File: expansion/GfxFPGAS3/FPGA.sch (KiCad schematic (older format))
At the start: 6 parts

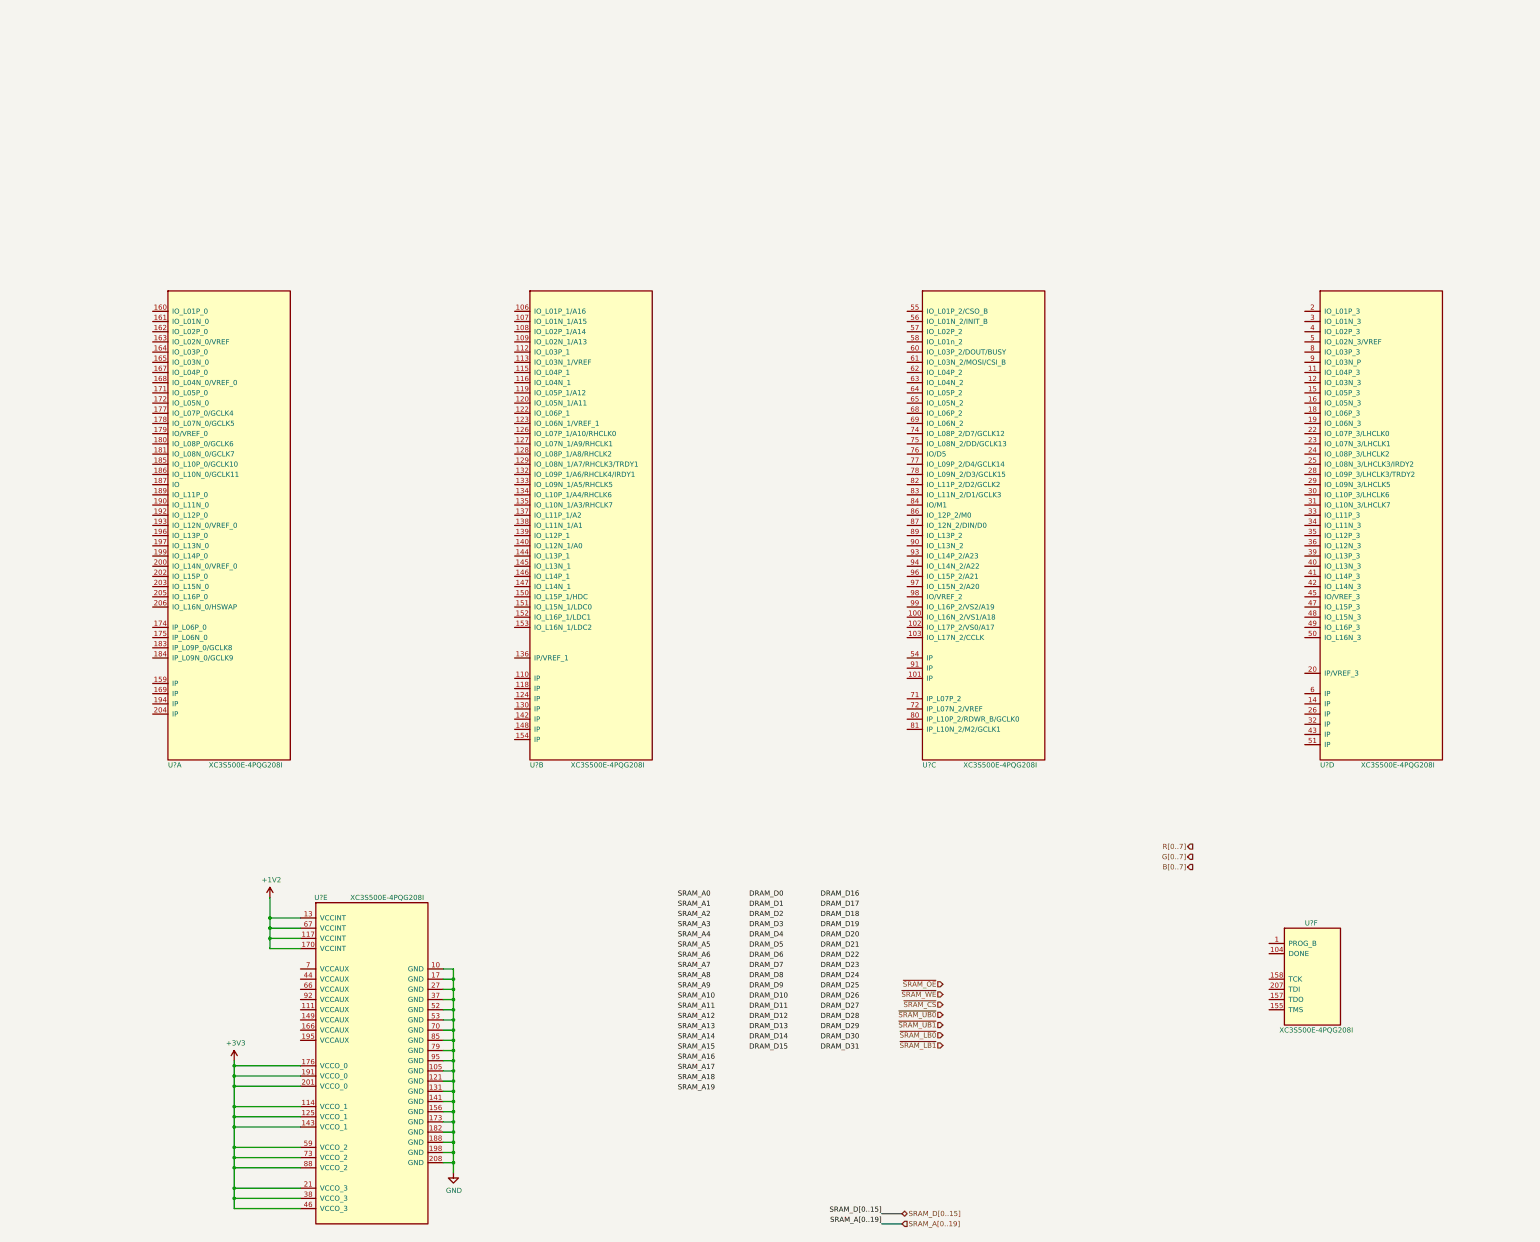
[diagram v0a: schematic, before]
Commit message: More progress on VGA card design
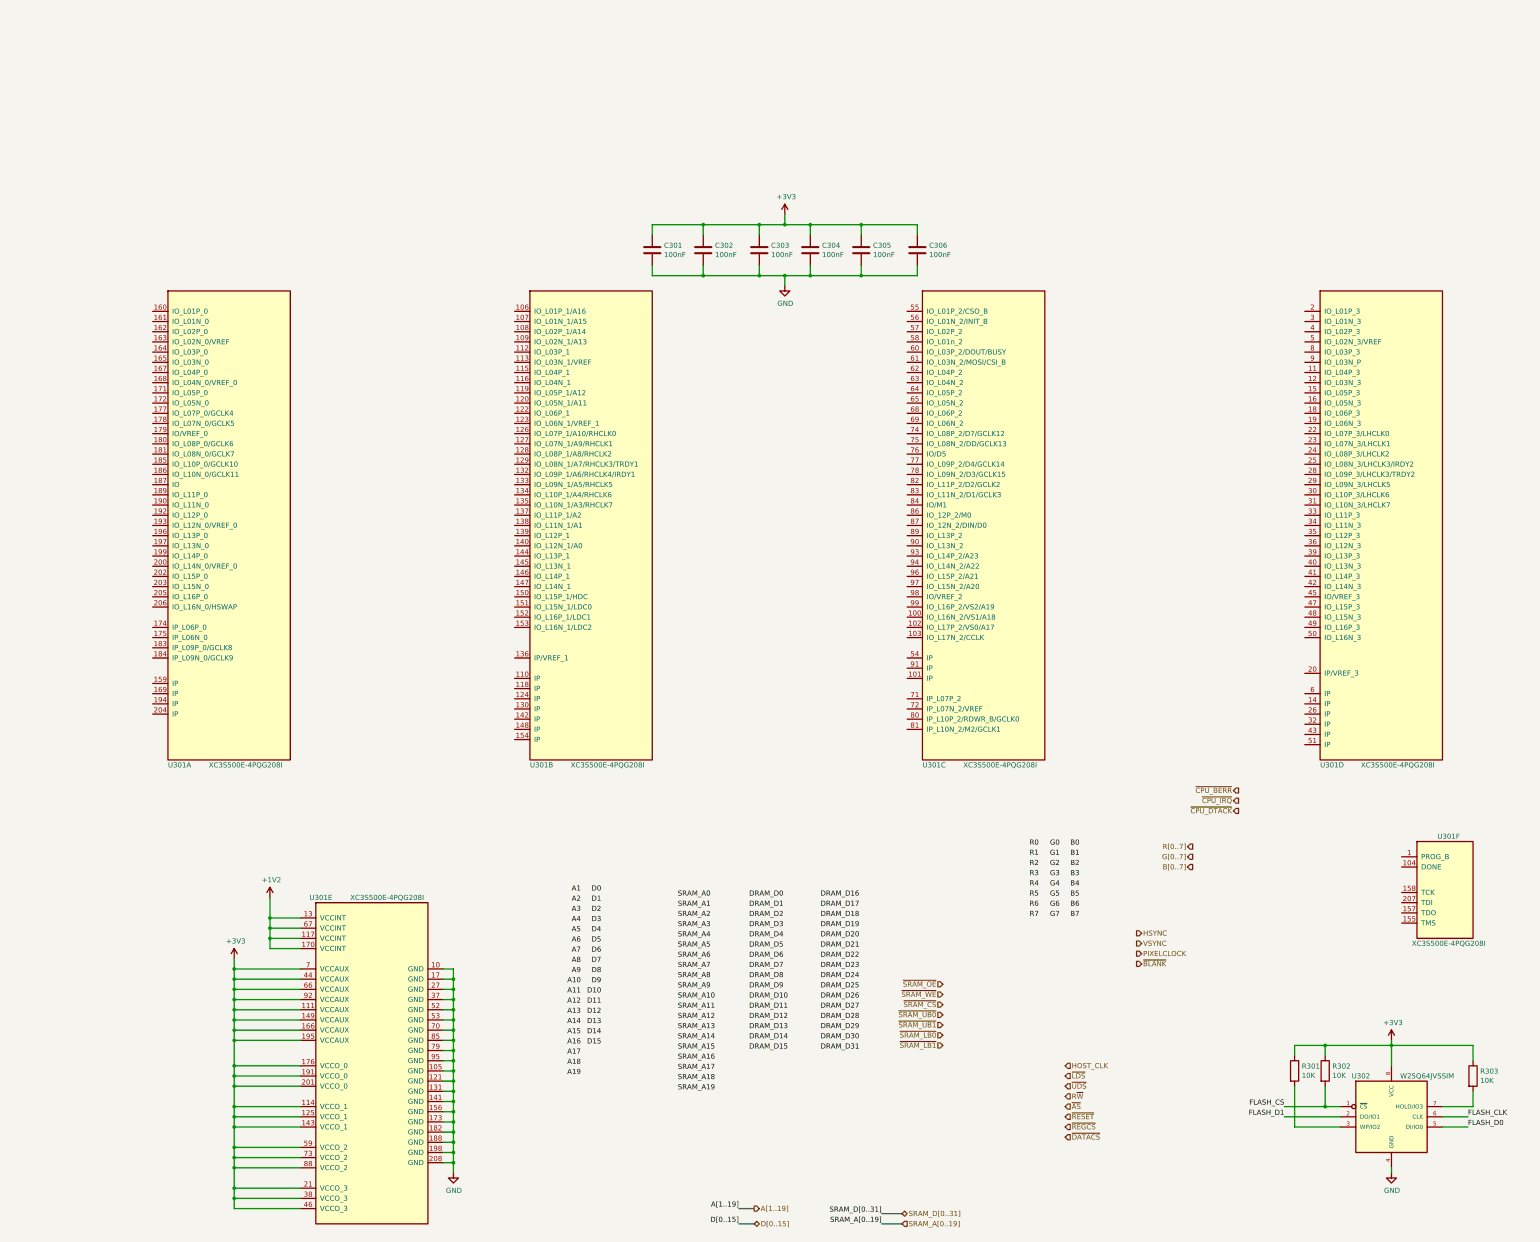
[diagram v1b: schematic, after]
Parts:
- added C301, C302, C303, C304, C305, C306: 100nF, Capacitor_SMD:C_0805_2012Metric, symbol Device:C
- added R301, R302, R303: 10K, Resistor_SMD:R_0805_2012Metric, symbol Device:R
- added U302: W25Q64JVSSIM, Ddraig:SOIC127P790X195-8N, symbol Ddraig:W25Q64JVSSIM
- U301: renamed from U?; footprint (none) -> Ddraig:QFP50P3060X3060X409-208N
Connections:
- net +3V3: now also U301.111 (VCCAUX), U301.149 (VCCAUX), U301.166 (VCCAUX), U301.195 (VCCAUX), U301.44 (VCCAUX), U301.66 (VCCAUX), U301.7 (VCCAUX), U301.92 (VCCAUX), C301.1, C302.1, C303.1, C304.1, C305.1, C306.1, R301.1, R302.1, R303.1, U302.8 (VCC)
- net GND: now also C301.2, C302.2, C303.2, C304.2, C305.2, C306.2, U302.4 (GND)
- new net: R301.2, U302.3 (WP/IO2)
- new net: R303.2, U302.7 (HOLD/IO3)
- new net FLASH_CLK: U302.6 (CLK)
- new net FLASH_CS: R302.2, U302.1 (~CS)
- new net FLASH_D0: U302.5 (DI/IO0)
- new net FLASH_D1: U302.2 (DO/IO1)
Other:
- moved on the sheet: U301F

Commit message: Started PCB layout
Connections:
- net B0: now also U301.129 (IO_L08N_1/A7/RHCLK3/TRDY1)
- net B1: now also U301.128 (IO_L08P_1/A8/RHCLK2)
- net B2: now also U301.127 (IO_L07N_1/A9/RHCLK1)
- net B3: now also U301.126 (IO_L07P_1/A10/RHCLK0)
- net B4: now also U301.123 (IO_L06N_1/VREF_1)
- net B5: now also U301.122 (IO_L06P_1)
- net B6: now also U301.120 (IO_L05N_1/A11)
- net B7: now also U301.119 (IO_L05P_1/A12)
- net G0: now also U301.140 (IO_L12N_1/A0)
- net G1: now also U301.139 (IO_L12P_1)
- net G2: now also U301.138 (IO_L11N_1/A1)
- net G3: now also U301.137 (IO_L11P_1/A2)
- net G4: now also U301.135 (IO_L10N_1/A3/RHCLK7)
- net G5: now also U301.134 (IO_L10P_1/A4/RHCLK6)
- net G6: now also U301.133 (IO_L09N_1/A5/RHCLK5)
- net G7: now also U301.132 (IO_L09P_1/A6/RHCLK4/IRDY1)
- net R0: now also U301.153 (IO_L16N_1/LDC2)
- net R1: now also U301.152 (IO_L16P_1/LDC1)
- net R2: now also U301.151 (IO_L15N_1/LDC0)
- net R3: now also U301.150 (IO_L15P_1/HDC)
- net R4: now also U301.147 (IO_L14N_1)
- net R5: now also U301.146 (IO_L14P_1)
- net R6: now also U301.145 (IO_L13N_1)
- net R7: now also U301.144 (IO_L13P_1)
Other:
- moved on the sheet: C301, C302, C303, C304, C305, C306, U301E, U301F

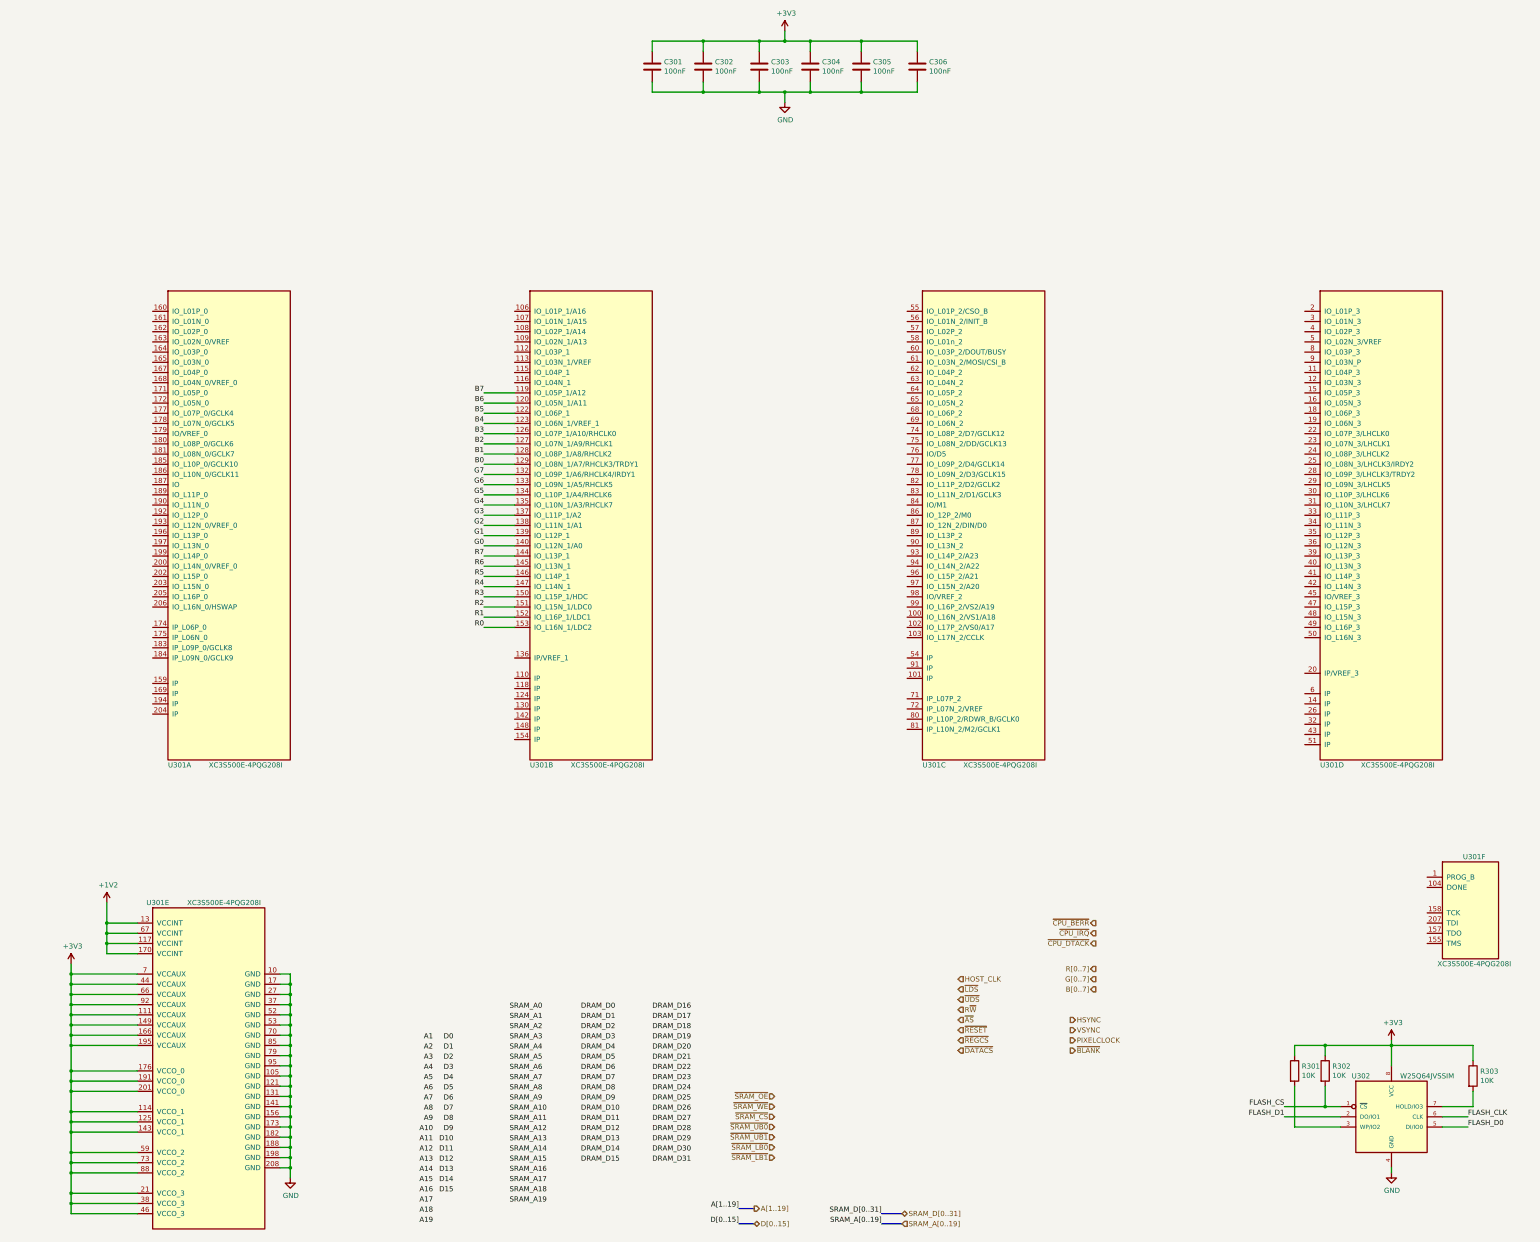
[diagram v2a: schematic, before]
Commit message: Improvements on bus wiring pinouts
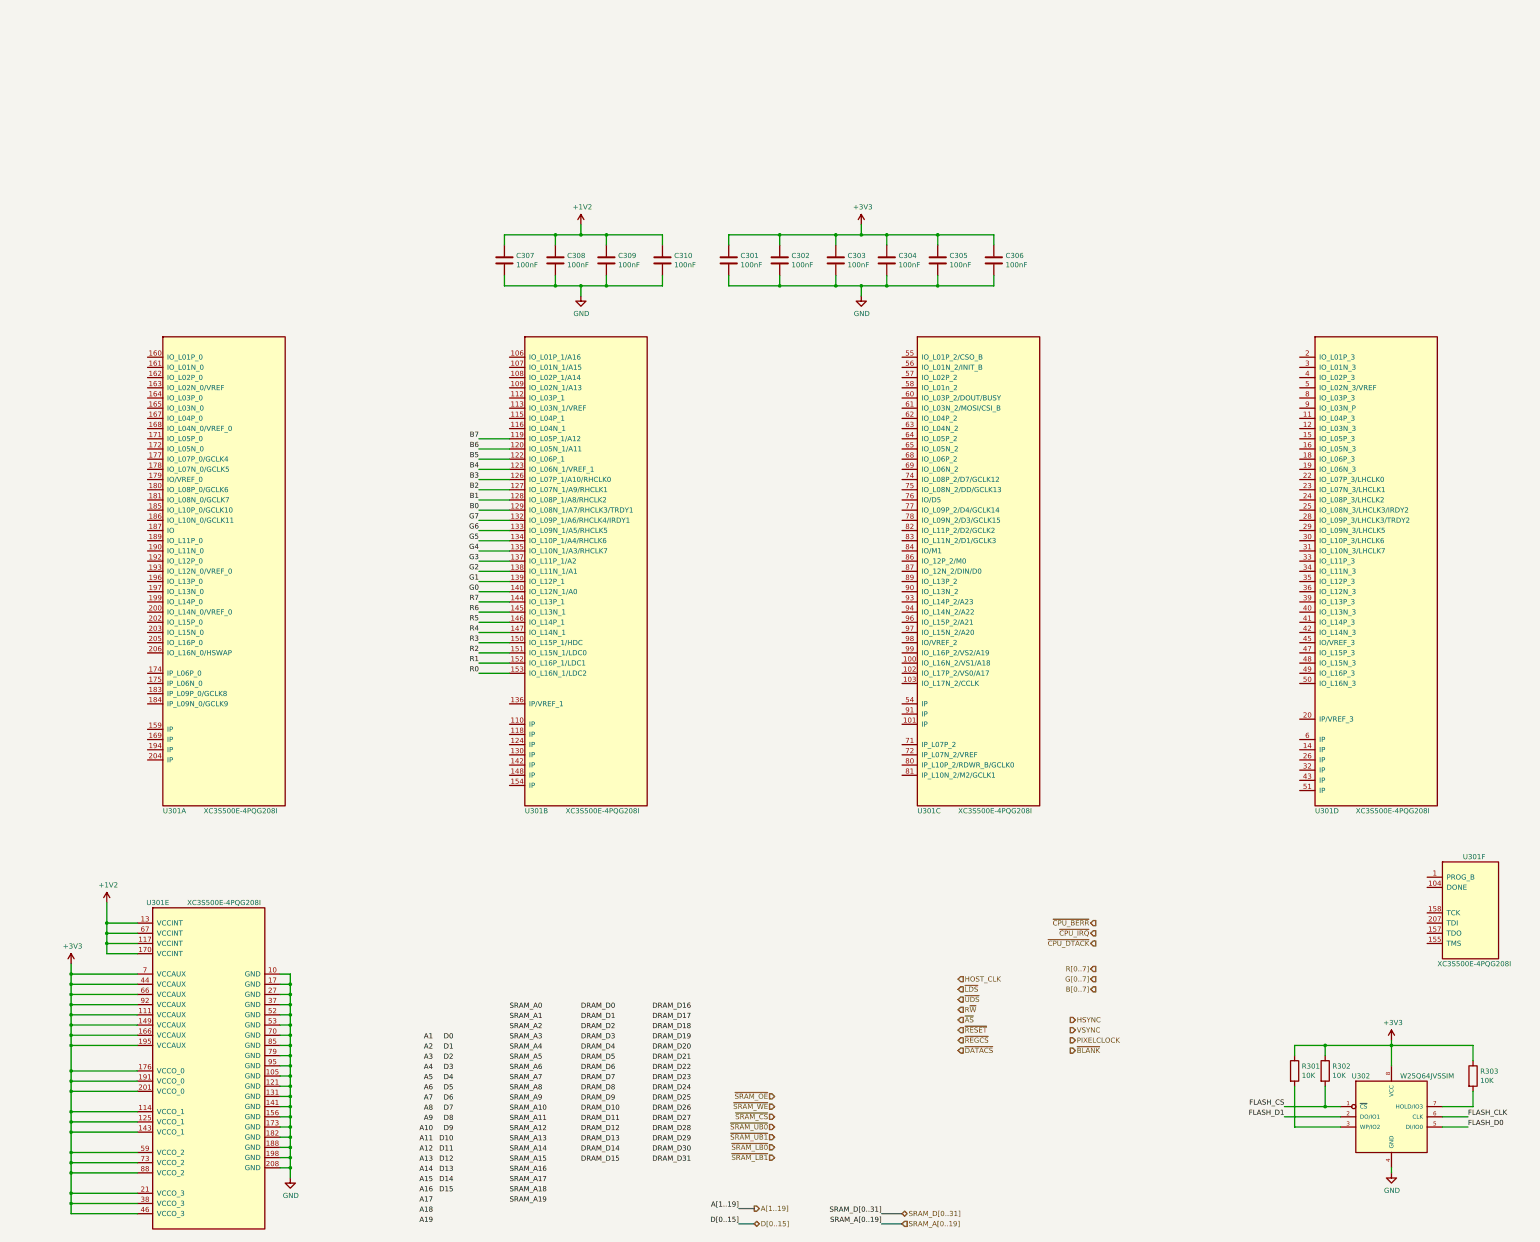
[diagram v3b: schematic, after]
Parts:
- added C307, C308, C309, C310: 100nF, Capacitor_SMD:C_0805_2012Metric, symbol Device:C
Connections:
- net +1V2: now also C307.1, C308.1, C309.1, C310.1
- net GND: now also C307.2, C308.2, C309.2, C310.2
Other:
- moved on the sheet: C301, C302, C303, C304, C305, C306, U301A, U301B, U301C, U301D
